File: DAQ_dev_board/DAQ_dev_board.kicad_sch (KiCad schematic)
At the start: 38 parts, among them J1 Thermocouple, J2 Conn_01x16_Pin, J3 Conn_01x08_Pin, J5 Conn_01x08_Pin, U1 ADS1158IRTCR (ADC), U2 AD8495 (TC AMP), U3 OP777ARZ (OP AMP), Y1 32.768kHz

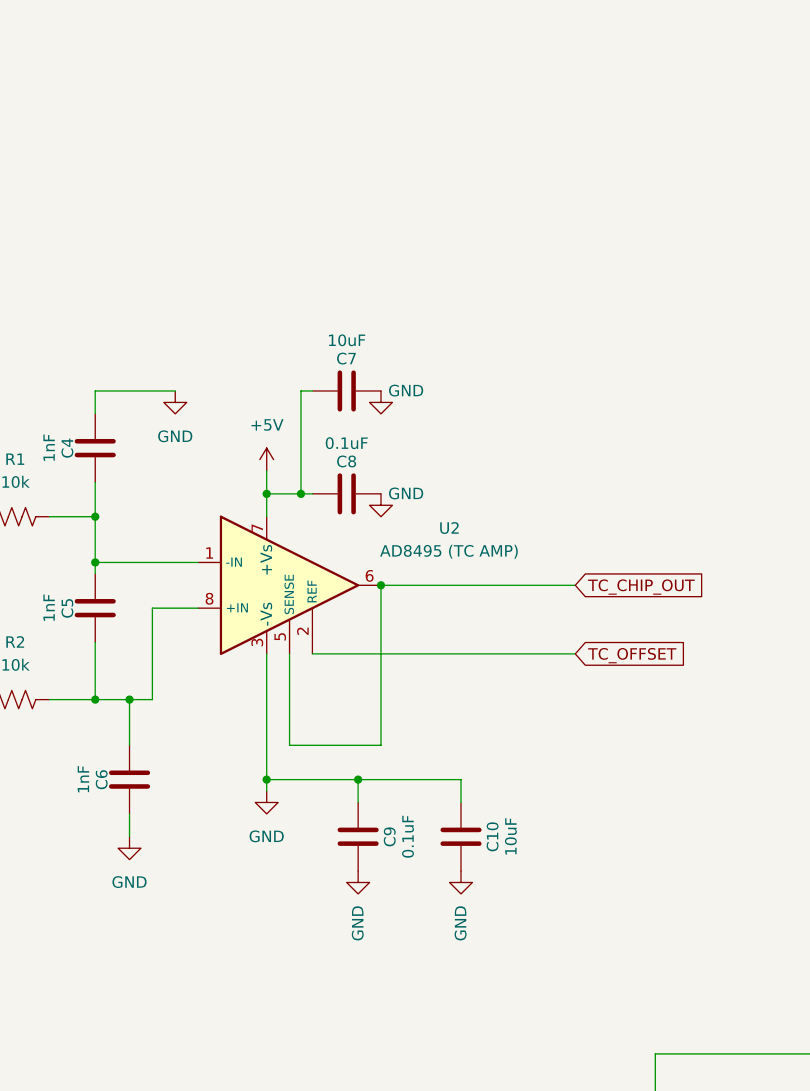
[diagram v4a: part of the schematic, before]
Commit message: updated DAQ schematic
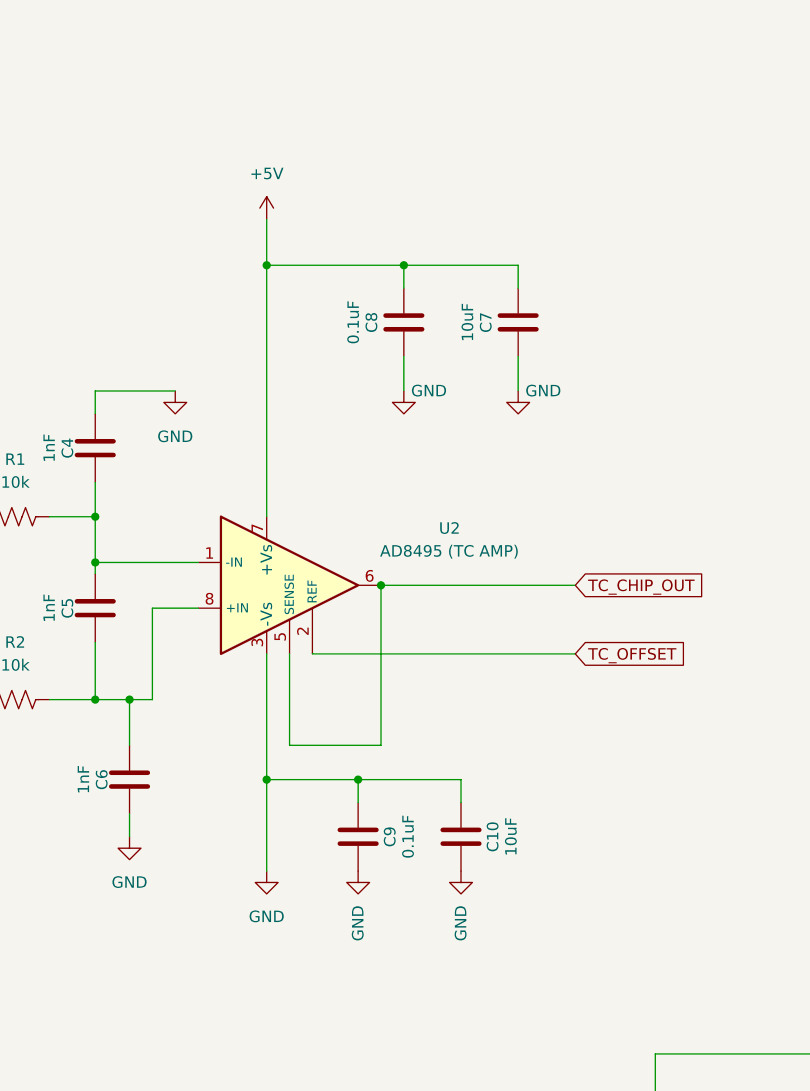
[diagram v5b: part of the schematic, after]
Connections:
- net +5V: now also C7.1, C8.1; no longer C7.2, C8.2
- net GND: now also C7.2, C8.2; no longer C7.1, C8.1
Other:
- moved on the sheet: C7, C8
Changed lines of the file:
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@@
 	)
 	(junction
-		(at 85.09 115.57)
-		(diameter 0)
-		(color 0 0 0 0)
-	)
-	(junction
 		(at 181.61 39.37)
 		(diameter 0)
@@
 	)
 	(junction
-		(at 81.28 115.57)
+		(at 287.02 107.95)
 		(diameter 0)
 		(color 0 0 0 0)
 	)
 	(junction
-		(at 287.02 107.95)
+		(at 346.71 72.39)
 		(diameter 0)
 		(color 0 0 0 0)
 	)
 	(junction
-		(at 346.71 72.39)
+		(at 339.09 48.26)
 		(diameter 0)
 		(color 0 0 0 0)
 	)
 	(junction
-		(at 339.09 48.26)
+		(at 81.28 90.17)
 		(diameter 0)
 		(color 0 0 0 0)
@@
 	)
 	(junction
+		(at 96.52 90.17)
+		(diameter 0)
+		(color 0 0 0 0)
+	)
+	(junction
 		(at 306.07 138.43)
 		(diameter 0)
@@
 	(wire
 		(pts
-			(xy 306.07 91.44) (xy 306.07 92.71)
+			(xy 81.28 90.17) (xy 96.52 90.17)
 		)
 		(stroke
@@
 	(wire
 		(pts
-			(xy 85.09 115.57) (xy 85.09 104.14)
+			(xy 306.07 91.44) (xy 306.07 92.71)
 		)
 		(stroke
@@
 	(wire
 		(pts
-			(xy 81.28 147.32) (xy 81.28 148.59)
+			(xy 81.28 147.32) (xy 81.28 157.48)
 		)
 		(stroke
@@
 	(wire
 		(pts
-			(xy 81.28 115.57) (xy 85.09 115.57)
+			(xy 96.52 90.17) (xy 96.52 92.71)
 		)
 		(stroke
@@
 	(wire
 		(pts
-			(xy 283.21 95.25) (xy 283.21 97.79)
+			(xy 96.52 90.17) (xy 109.22 90.17)
 		)
 		(stroke
@@
 	(wire
 		(pts
-			(xy 85.09 115.57) (xy 86.36 115.57)
+			(xy 283.21 95.25) (xy 283.21 97.79)
 		)
 		(stroke
@@
 	(wire
 		(pts
+			(xy 109.22 100.33) (xy 109.22 104.14)
+		)
+		(stroke
+			(width 0)
+			(type default)
+		)
+	)
+	(wire
+		(pts
 			(xy 283.21 100.33) (xy 289.56 100.33)
 		)
@@
 	(wire
 		(pts
-			(xy 85.09 104.14) (xy 86.36 104.14)
-		)
-		(stroke
-			(width 0)
-			(type default)
-		)
-	)
-	(wire
-		(pts
 			(xy 288.29 77.47) (xy 292.1 77.47)
 		)
@@
 	(wire
 		(pts
-			(xy 81.28 113.03) (xy 81.28 115.57)
-		)
-		(stroke
-			(width 0)
-			(type default)
-		)
-	)
-	(wire
-		(pts
 			(xy 354.33 55.88) (xy 354.33 74.93)
 		)
@@
 	(wire
 		(pts
-			(xy 81.28 115.57) (xy 81.28 118.11)
+			(xy 81.28 90.17) (xy 81.28 118.11)
 		)
 		(stroke
@@
 	(wire
 		(pts
+			(xy 81.28 85.09) (xy 81.28 90.17)
+		)
+		(stroke
+			(width 0)
+			(type default)
+		)
+	)
+	(wire
+		(pts
 			(xy 339.09 69.85) (xy 370.84 69.85)
 		)
@@
 	(wire
 		(pts
+			(xy 109.22 90.17) (xy 109.22 92.71)
+		)
+		(stroke
+			(width 0)
+			(type default)
+		)
+	)
+	(wire
+		(pts
 			(xy 346.71 72.39) (xy 370.84 72.39)
 		)
@@
 	(wire
 		(pts
+			(xy 96.52 100.33) (xy 96.52 104.14)
+		)
+		(stroke
+			(width 0)
+			(type default)
+		)
+	)
+	(wire
+		(pts
 			(xy 181.61 50.8) (xy 171.45 50.8)
 		)
@@
 	(symbol
 		(lib_id "Device:C")
-		(at 90.17 104.14 270)
+		(at 109.22 96.52 0)
 		(unit 1)
 		(exclude_from_sim no)
@@
 		(dnp no)
 		(property "Reference" "C7"
-			(at 90.17 100.584 90)
+			(at 105.664 96.52 90)
 			(effects
 				(font
@@
 		)
 		(property "Value" "10uF"
-			(at 90.17 98.552 90)
+			(at 103.632 96.52 90)
 			(effects
 				(font
@@
 		)
 		(property "Footprint" "Capacitor_SMD:C_0603_1608Metric"
-			(at 86.36 105.1052 0)
+			(at 110.1852 100.33 0)
 			(effects
 				(font
@@
 		)
 		(property "Datasheet" "~"
-			(at 90.17 104.14 0)
+			(at 109.22 96.52 0)
 			(effects
 				(font
@@
 		)
 		(property "Description" "Unpolarized capacitor"
-			(at 90.17 104.14 0)
+			(at 109.22 96.52 0)
 			(effects
 				(font
@@
 	(symbol
 		(lib_id "power:+5V")
-		(at 81.28 113.03 0)
+		(at 81.28 85.09 0)
 		(unit 1)
 		(exclude_from_sim no)
@@
 		(fields_autoplaced yes)
 		(property "Reference" "#PWR08"
-			(at 81.28 116.84 0)
+			(at 81.28 88.9 0)
 			(effects
 				(font
@@
 		)
 		(property "Value" "+5V"
-			(at 81.28 107.95 0)
+			(at 81.28 80.01 0)
 			(effects
 				(font
@@
 		)
 		(property "Footprint" ""
-			(at 81.28 113.03 0)
+			(at 81.28 85.09 0)
 			(effects
 				(font
@@
 		)
 		(property "Datasheet" ""
-			(at 81.28 113.03 0)
+			(at 81.28 85.09 0)
 			(effects
 				(font
@@
 		)
 		(property "Description" "Power symbol creates a global label with name \"+5V\""
-			(at 81.28 113.03 0)
+			(at 81.28 85.09 0)
 			(effects
 				(font
@@
 	(symbol
 		(lib_id "power:GND")
-		(at 81.28 148.59 0)
+		(at 81.28 157.48 0)
 		(unit 1)
 		(exclude_from_sim no)
@@
 		(fields_autoplaced yes)
 		(property "Reference" "#PWR012"
-			(at 81.28 154.94 0)
+			(at 81.28 163.83 0)
 			(effects
 				(font
@@
 		)
 		(property "Value" "GND"
-			(at 81.28 153.67 0)
+			(at 81.28 162.56 0)
 			(effects
 				(font
@@
 		)
 		(property "Footprint" ""
-			(at 81.28 148.59 0)
+			(at 81.28 157.48 0)
 			(effects
 				(font
@@
 		)
 		(property "Datasheet" ""
-			(at 81.28 148.59 0)
+			(at 81.28 157.48 0)
 			(effects
 				(font
@@
 		)
 		(property "Description" "Power symbol creates a global label with name \"GND\" , ground"
-			(at 81.28 148.59 0)
+			(at 81.28 157.48 0)
 			(effects
 				(font
@@
 	(symbol
 		(lib_id "power:GND")
-		(at 93.98 104.14 0)
+		(at 109.22 104.14 0)
 		(unit 1)
 		(exclude_from_sim no)
@@
 		(dnp no)
 		(property "Reference" "#PWR010"
-			(at 93.98 110.49 0)
+			(at 109.22 110.49 0)
 			(effects
 				(font
@@
 		)
 		(property "Value" "GND"
-			(at 96.774 104.14 0)
+			(at 112.014 104.14 0)
 			(effects
 				(font
@@
 		)
 		(property "Footprint" ""
-			(at 93.98 104.14 0)
+			(at 109.22 104.14 0)
 			(effects
 				(font
@@
 		)
 		(property "Datasheet" ""
-			(at 93.98 104.14 0)
+			(at 109.22 104.14 0)
 			(effects
 				(font
@@
 		)
 		(property "Description" "Power symbol creates a global label with name \"GND\" , ground"
-			(at 93.98 104.14 0)
+			(at 109.22 104.14 0)
 			(effects
 				(font
@@
 	(symbol
 		(lib_id "Device:C")
-		(at 90.17 115.57 270)
+		(at 96.52 96.52 0)
 		(unit 1)
 		(exclude_from_sim no)
@@
 		(dnp no)
 		(property "Reference" "C8"
-			(at 90.17 112.014 90)
+			(at 92.964 96.52 90)
 			(effects
 				(font
@@
 		)
 		(property "Value" "0.1uF"
-			(at 90.17 109.982 90)
+			(at 90.932 96.52 90)
 			(effects
 				(font
@@
 		)
 		(property "Footprint" "Capacitor_SMD:C_0603_1608Metric"
-			(at 86.36 116.5352 0)
+			(at 97.4852 100.33 0)
 			(effects
 				(font
@@
 		)
 		(property "Datasheet" "~"
-			(at 90.17 115.57 0)
+			(at 96.52 96.52 0)
 			(effects
 				(font
@@
 		)
 		(property "Description" "Unpolarized capacitor"
-			(at 90.17 115.57 0)
+			(at 96.52 96.52 0)
 			(effects
 				(font
@@
 	(symbol
 		(lib_id "power:GND")
-		(at 93.98 115.57 0)
+		(at 96.52 104.14 0)
 		(unit 1)
 		(exclude_from_sim no)
@@
 		(dnp no)
 		(property "Reference" "#PWR011"
-			(at 93.98 121.92 0)
+			(at 96.52 110.49 0)
 			(effects
 				(font
@@
 		)
 		(property "Value" "GND"
-			(at 96.774 115.57 0)
+			(at 99.314 104.14 0)
 			(effects
 				(font
@@
 		)
 		(property "Footprint" ""
-			(at 93.98 115.57 0)
+			(at 96.52 104.14 0)
 			(effects
 				(font
@@
 		)
 		(property "Datasheet" ""
-			(at 93.98 115.57 0)
+			(at 96.52 104.14 0)
 			(effects
 				(font
@@
 		)
 		(property "Description" "Power symbol creates a global label with name \"GND\" , ground"
-			(at 93.98 115.57 0)
+			(at 96.52 104.14 0)
 			(effects
 				(font

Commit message: sync
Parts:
- R1, R10, R11, R12, R13, R14, R2, R3, R4, R5, R6, R7, R8, R9: footprint Resistor_SMD:R_0201_0603Metric -> Resistor_SMD:R_0603_1608Metric
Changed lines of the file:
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@@
 			)
 		)
-		(property "Footprint" "Resistor_SMD:R_0201_0603Metric"
+		(property "Footprint" "Resistor_SMD:R_0603_1608Metric"
 			(at 119.126 200.914 90)
 			(effects
@@
 			)
 		)
-		(property "Footprint" "Resistor_SMD:R_0201_0603Metric"
+		(property "Footprint" "Resistor_SMD:R_0603_1608Metric"
 			(at 340.106 52.324 90)
 			(effects
@@
 			)
 		)
-		(property "Footprint" "Resistor_SMD:R_0201_0603Metric"
+		(property "Footprint" "Resistor_SMD:R_0603_1608Metric"
 			(at 119.126 222.504 90)
 			(effects
@@
 			)
 		)
-		(property "Footprint" "Resistor_SMD:R_0201_0603Metric"
+		(property "Footprint" "Resistor_SMD:R_0603_1608Metric"
 			(at 347.726 52.324 90)
 			(effects
@@
 			)
 		)
-		(property "Footprint" "Resistor_SMD:R_0201_0603Metric"
+		(property "Footprint" "Resistor_SMD:R_0603_1608Metric"
 			(at 53.594 117.094 90)
 			(effects
@@
 			)
 		)
-		(property "Footprint" "Resistor_SMD:R_0201_0603Metric"
+		(property "Footprint" "Resistor_SMD:R_0603_1608Metric"
 			(at 355.346 52.324 90)
 			(effects
@@
 			)
 		)
-		(property "Footprint" "Resistor_SMD:R_0201_0603Metric"
+		(property "Footprint" "Resistor_SMD:R_0603_1608Metric"
 			(at 154.686 47.244 90)
 			(effects
@@
 			)
 		)
-		(property "Footprint" "Resistor_SMD:R_0201_0603Metric"
+		(property "Footprint" "Resistor_SMD:R_0603_1608Metric"
 			(at 280.924 47.244 90)
 			(effects
@@
 			)
 		)
-		(property "Footprint" "Resistor_SMD:R_0201_0603Metric"
+		(property "Footprint" "Resistor_SMD:R_0603_1608Metric"
 			(at 324.866 52.324 90)
 			(effects
@@
 			)
 		)
-		(property "Footprint" "Resistor_SMD:R_0201_0603Metric"
+		(property "Footprint" "Resistor_SMD:R_0603_1608Metric"
 			(at 35.814 110.744 90)
 			(effects
@@
 			)
 		)
-		(property "Footprint" "Resistor_SMD:R_0201_0603Metric"
+		(property "Footprint" "Resistor_SMD:R_0603_1608Metric"
 			(at 309.626 52.324 90)
 			(effects
@@
 			)
 		)
-		(property "Footprint" "Resistor_SMD:R_0201_0603Metric"
+		(property "Footprint" "Resistor_SMD:R_0603_1608Metric"
 			(at 332.486 52.324 90)
 			(effects
@@
 			)
 		)
-		(property "Footprint" "Resistor_SMD:R_0201_0603Metric"
+		(property "Footprint" "Resistor_SMD:R_0603_1608Metric"
 			(at 53.594 137.414 90)
 			(effects
@@
 			)
 		)
-		(property "Footprint" "Resistor_SMD:R_0201_0603Metric"
+		(property "Footprint" "Resistor_SMD:R_0603_1608Metric"
 			(at 317.246 52.324 90)
 			(effects
